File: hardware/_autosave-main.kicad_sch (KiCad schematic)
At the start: 15 parts, among them J3 Conn_01x01_Pin, J4 Conn_01x01_Pin, J5 Conn_01x01_Pin, J6 Conn_01x01_Pin, K2 ADW11

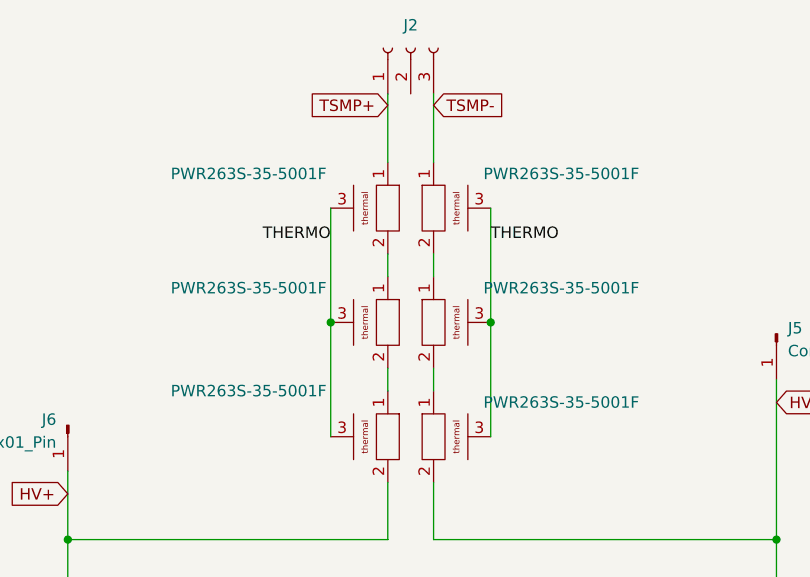
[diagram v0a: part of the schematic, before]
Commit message: changed resistors
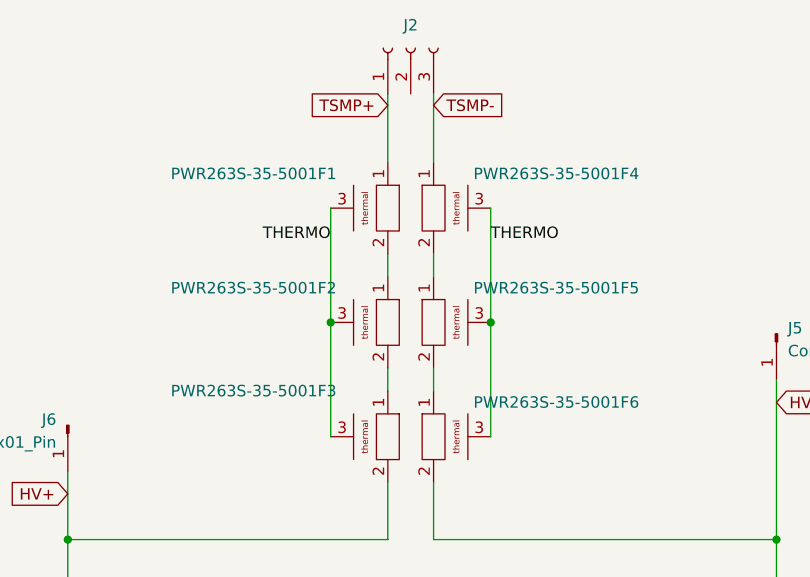
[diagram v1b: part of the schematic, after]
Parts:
- PWR263S-35-5001F1, PWR263S-35-5001F2, PWR263S-35-5001F3, PWR263S-35-5001F4, PWR263S-35-5001F5, PWR263S-35-5001F6: renamed from PWR263S-35-5001F; footprint (none) -> 7696:PWR263S-35-5001F
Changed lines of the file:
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@@
   (symbol (lib_id "7696:PWR263S-35-5001F") (at 74.93 80.01 0) (unit 1)
     (in_bom yes) (on_board yes) (dnp no)
-    (property "Reference" "PWR263S-35-5001F" (at 99.06 73.66 0)
+    (property "Reference" "PWR263S-35-5001F6" (at 99.06 73.66 0)
       (effects (font (size 1.27 1.27)) (justify right))
     )
@@
       (effects (font (size 1.27 1.27)))
     )
-    (property "Footprint" "" (at 74.93 80.01 0)
+    (property "Footprint" "7696:PWR263S-35-5001F" (at 74.93 80.01 0)
       (effects (font (size 1.27 1.27)) hide)
     )
@@
       (project "main"
         (path "/b652b05a-4e3d-4ad1-b032-18886abe7d45"
-          (reference "PWR263S-35-5001F") (unit 1)
+          (reference "PWR263S-35-5001F6") (unit 1)
         )
       )
@@
   (symbol (lib_id "7696:PWR263S-35-5001F") (at 74.93 67.31 0) (unit 1)
     (in_bom yes) (on_board yes) (dnp no)
-    (property "Reference" "PWR263S-35-5001F" (at 99.06 60.96 0)
+    (property "Reference" "PWR263S-35-5001F5" (at 99.06 60.96 0)
       (effects (font (size 1.27 1.27)) (justify right))
     )
@@
       (effects (font (size 1.27 1.27)))
     )
-    (property "Footprint" "" (at 74.93 67.31 0)
+    (property "Footprint" "7696:PWR263S-35-5001F" (at 74.93 67.31 0)
       (effects (font (size 1.27 1.27)) hide)
     )
@@
       (project "main"
         (path "/b652b05a-4e3d-4ad1-b032-18886abe7d45"
-          (reference "PWR263S-35-5001F") (unit 1)
+          (reference "PWR263S-35-5001F5") (unit 1)
         )
       )
@@
   (symbol (lib_id "7696:PWR263S-35-5001F") (at 72.39 54.61 0) (mirror y) (unit 1)
     (in_bom yes) (on_board yes) (dnp no)
-    (property "Reference" "PWR263S-35-5001F" (at 46.99 48.26 0)
+    (property "Reference" "PWR263S-35-5001F1" (at 46.99 48.26 0)
       (effects (font (size 1.27 1.27)) (justify right))
     )
@@
       (effects (font (size 1.27 1.27)))
     )
-    (property "Footprint" "" (at 72.39 54.61 0)
+    (property "Footprint" "7696:PWR263S-35-5001F" (at 72.39 54.61 0)
       (effects (font (size 1.27 1.27)) hide)
     )
@@
       (project "main"
         (path "/b652b05a-4e3d-4ad1-b032-18886abe7d45"
-          (reference "PWR263S-35-5001F") (unit 1)
+          (reference "PWR263S-35-5001F1") (unit 1)
         )
       )
@@
   (symbol (lib_id "7696:PWR263S-35-5001F") (at 72.39 67.31 0) (mirror y) (unit 1)
     (in_bom yes) (on_board yes) (dnp no)
-    (property "Reference" "PWR263S-35-5001F" (at 46.99 60.96 0)
+    (property "Reference" "PWR263S-35-5001F2" (at 46.99 60.96 0)
       (effects (font (size 1.27 1.27)) (justify right))
     )
@@
       (effects (font (size 1.27 1.27)))
     )
-    (property "Footprint" "" (at 72.39 67.31 0)
+    (property "Footprint" "7696:PWR263S-35-5001F" (at 72.39 67.31 0)
       (effects (font (size 1.27 1.27)) hide)
     )
@@
       (project "main"
         (path "/b652b05a-4e3d-4ad1-b032-18886abe7d45"
-          (reference "PWR263S-35-5001F") (unit 1)
+          (reference "PWR263S-35-5001F2") (unit 1)
         )
       )
@@
   (symbol (lib_id "7696:PWR263S-35-5001F") (at 72.39 80.01 0) (mirror y) (unit 1)
     (in_bom yes) (on_board yes) (dnp no)
-    (property "Reference" "PWR263S-35-5001F" (at 46.99 72.39 0)
+    (property "Reference" "PWR263S-35-5001F3" (at 46.99 72.39 0)
       (effects (font (size 1.27 1.27)) (justify right))
     )
@@
       (effects (font (size 1.27 1.27)))
     )
-    (property "Footprint" "" (at 72.39 80.01 0)
+    (property "Footprint" "7696:PWR263S-35-5001F" (at 72.39 80.01 0)
       (effects (font (size 1.27 1.27)) hide)
     )
@@
       (project "main"
         (path "/b652b05a-4e3d-4ad1-b032-18886abe7d45"
-          (reference "PWR263S-35-5001F") (unit 1)
+          (reference "PWR263S-35-5001F3") (unit 1)
         )
       )
@@
   (symbol (lib_id "7696:PWR263S-35-5001F") (at 74.93 54.61 0) (unit 1)
     (in_bom yes) (on_board yes) (dnp no)
-    (property "Reference" "PWR263S-35-5001F" (at 99.06 48.26 0)
+    (property "Reference" "PWR263S-35-5001F4" (at 99.06 48.26 0)
       (effects (font (size 1.27 1.27)) (justify right))
     )
@@
       (effects (font (size 1.27 1.27)))
     )
-    (property "Footprint" "" (at 74.93 54.61 0)
+    (property "Footprint" "7696:PWR263S-35-5001F" (at 74.93 54.61 0)
       (effects (font (size 1.27 1.27)) hide)
     )
@@
       (project "main"
         (path "/b652b05a-4e3d-4ad1-b032-18886abe7d45"
-          (reference "PWR263S-35-5001F") (unit 1)
-        )
-      )
+          (reference "PWR263S-35-5001F4") (unit 1)
+        )
+      )
